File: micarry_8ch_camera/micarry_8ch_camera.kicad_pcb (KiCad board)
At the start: 2 copper layers, 127.2 x 127.2 mm, 68 parts, among them IC1 74LCX125MTCX, IC2 74LCX125MTCX, J1 MCHStreamer J3

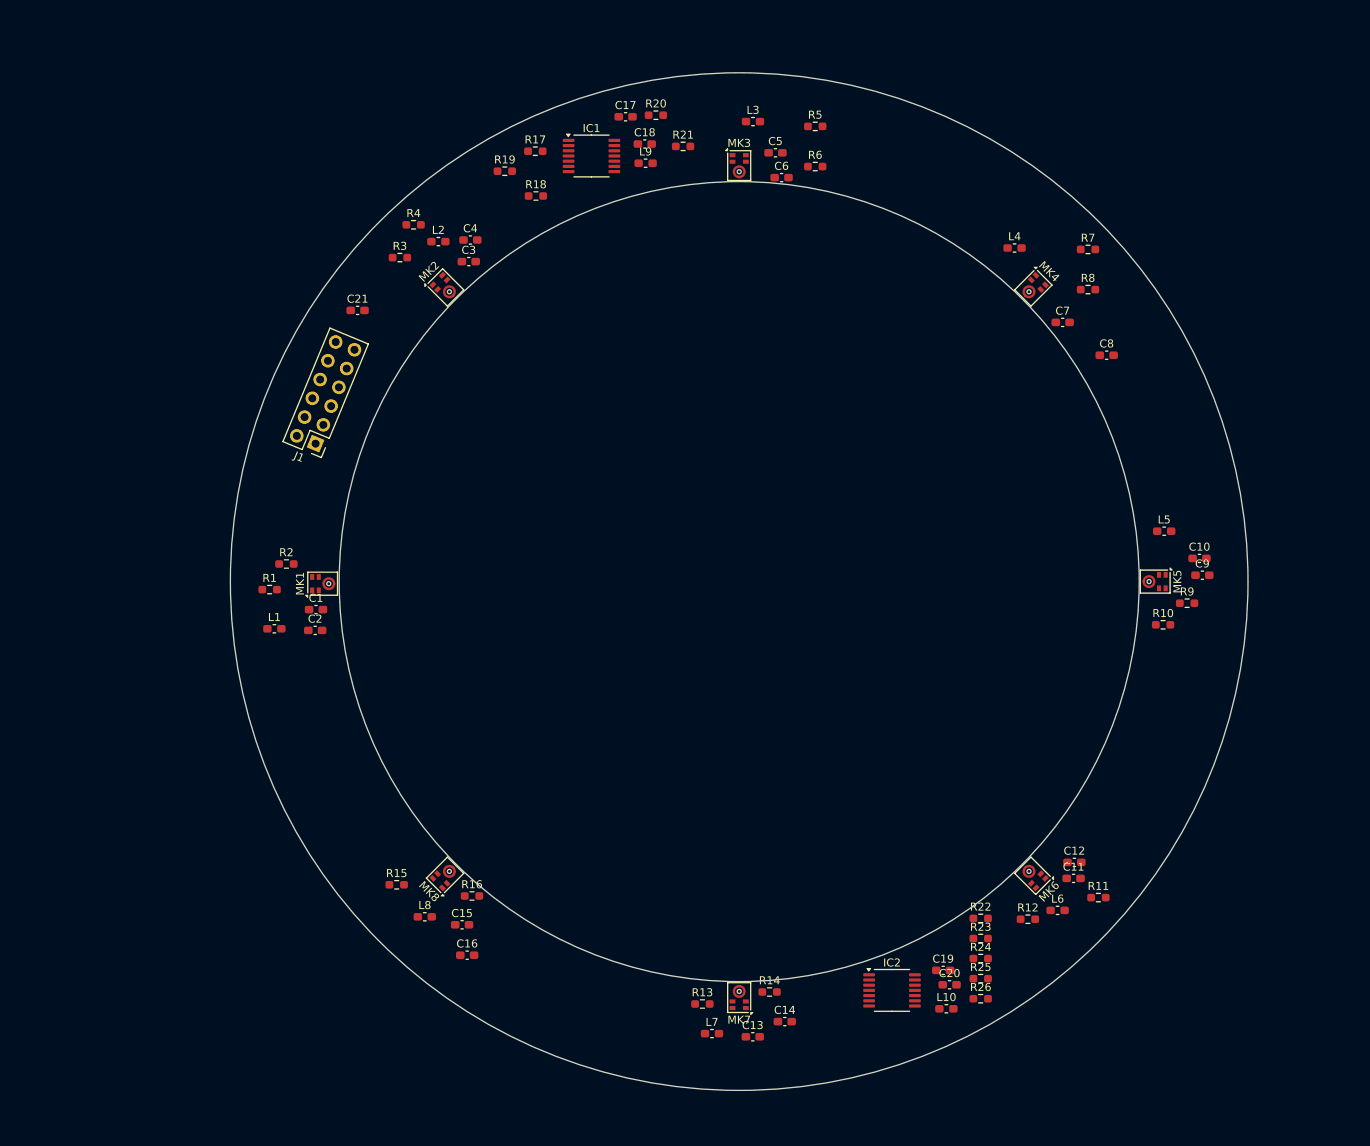
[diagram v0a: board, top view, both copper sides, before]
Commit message: 8ch progress, new mics for 16ch
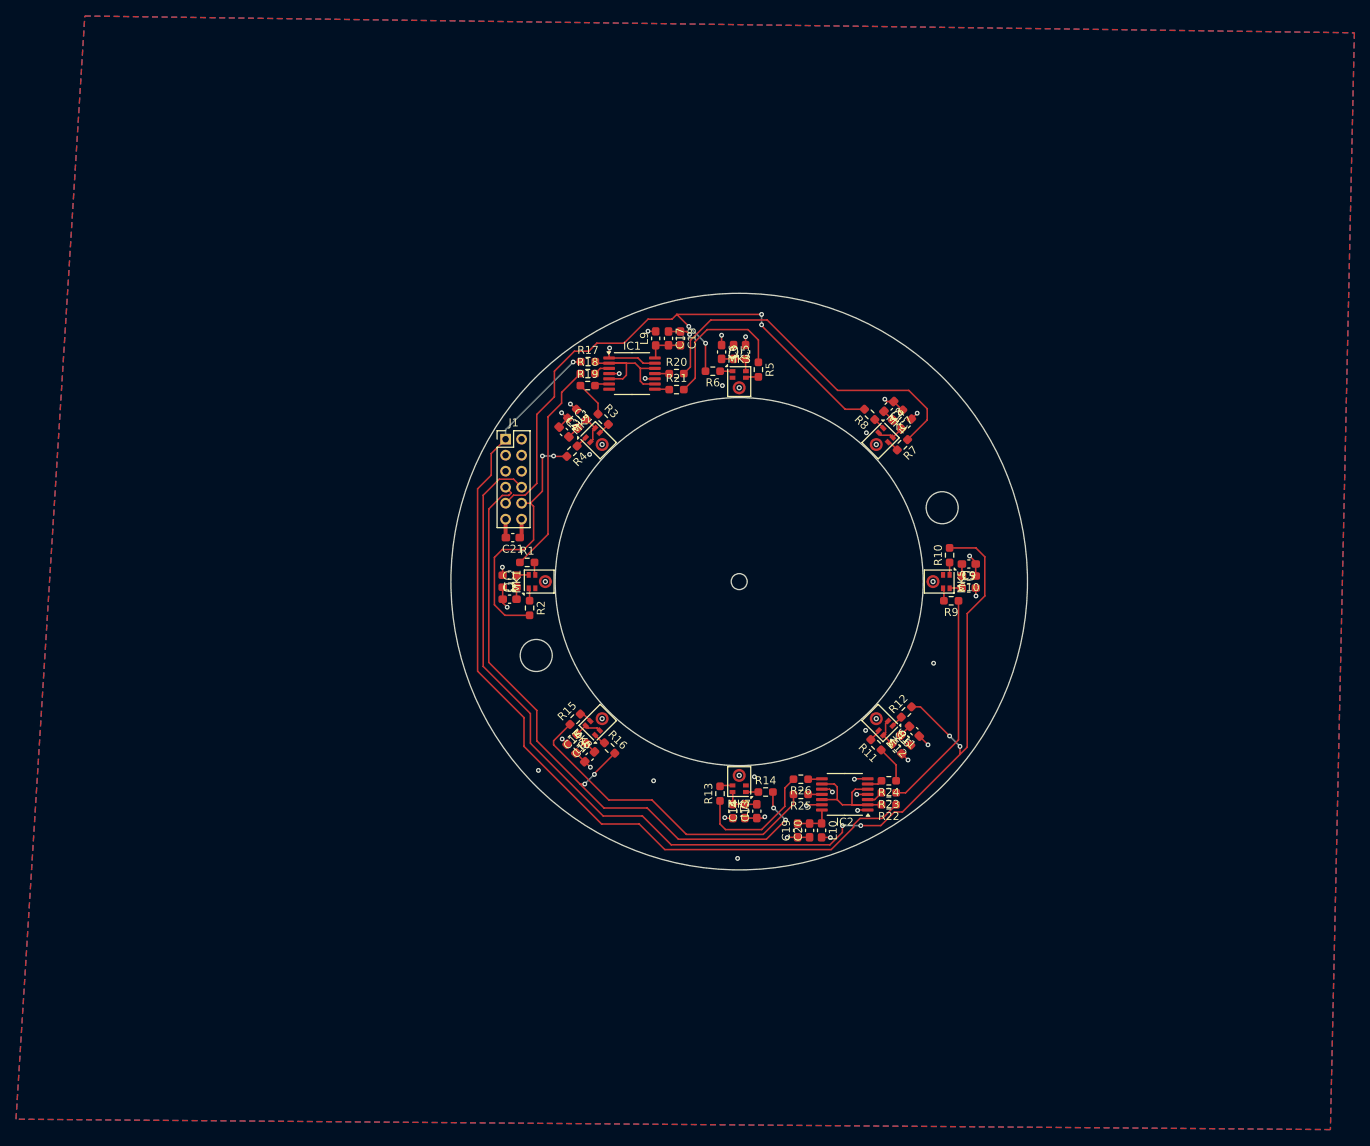
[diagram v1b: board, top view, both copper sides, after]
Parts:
- J1: footprint Connector_PinHeader_2.54mm:PinHeader_2x06_P2.54mm_Vertical -> Connector_PinHeader_2.00mm:PinHeader_2x06_P2.00mm_Vertical
- moved R26 35.5 mm to (157.7, 124.7), turned to 180 degrees
- moved R4 34.5 mm to (129.1, 83.7), turned to -135 degrees
- moved C21 34.4 mm to (121.7, 94.5), turned to 180 degrees
- moved R11 33.7 mm to (167.1, 120.4), turned to 135 degrees
- moved R7 33.7 mm to (170.4, 82.9), turned to -135 degrees
- moved R3 32.5 mm to (133.0, 79.7), turned to -45 degrees
- moved R20 32.4 mm to (142.2, 74.0)
- moved R1 32.4 mm to (123.5, 97.6)
- moved R25 32.2 mm to (157.7, 126.6), turned to 180 degrees
- moved R8 31.4 mm to (166.3, 79.1), turned to 135 degrees
- moved R5 31.2 mm to (152.4, 73.5), turned to -90 degrees
- moved R2 30.9 mm to (123.8, 103.3), turned to -90 degrees
- moved R15 30.4 mm to (129.5, 117.2), turned to 45 degrees
- moved R21 30.4 mm to (142.2, 76.0)
- moved L1 30.2 mm to (121.3, 99.2), turned to 180 degrees
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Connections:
- R18 pad 1: PDM_CLK1 -> PDM_CLK0
- R19 pad 1: PDM_CLK0 -> PDM_CLK1
- R23 pad 1: PDM_CLK5 -> PDM_CLK4
- R24 pad 1: PDM_CLK4 -> PDM_CLK5
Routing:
- net PDM_DATA2: track 0.00 -> 143.6 mm, vias 0 -> 4
- net PDM_CLK-IN: track 0.00 -> 110.7 mm, vias 0 -> 1
- net PDM_DATA3: track 0.00 -> 83.5 mm, vias 0 -> 4
- net PDM_DATA1: track 0.00 -> 75.9 mm, vias 0 -> 4
- net PDM_CLK3: track 0.00 -> 44.6 mm
- net GND: track 0.00 -> 44.4 mm, vias 0 -> 27
- net PDM_CLK7: track 0.00 -> 40.8 mm
- net PDM_DATA0: track 0.00 -> 32.1 mm, vias 0 -> 2
- net PDM_CLK4: track 0.00 -> 27.9 mm
- net PDM_CLK0: track 0.00 -> 26.7 mm
- net PDM_CLK2: track 0.00 -> 18.4 mm
- net Net-(IC1-A0): track 0.00 -> 17.4 mm
- net Net-(IC2-A0): track 0.00 -> 17.0 mm
- net PDM_CLK6: track 0.00 -> 16.3 mm
- net +3V3: track 0.00 -> 12.7 mm, vias 0 -> 10
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- added copper zone on In2.Cu, net +3V3
- added copper zone on B.Cu, net GND
- added copper zone on F.Cu, net GND
- added copper zone on In1.Cu, net GND
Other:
- board size 127.2 x 127.2 mm -> 72.1 x 72.1 mm
- copper layers 2 -> 4

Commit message: Save before dev-fork
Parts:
- MK1, MK2, MK3, MK4, MK5, MK6, MK7, MK8: value SPH1668LM4H-1 -> ~; footprint Sensor_Audio:Knowles_LGA-5_3.5x2.65mm -> ul_IM73D122V01XTMA1:PG-LLGA-5-2_INF
- moved C21 6.62 mm to (116.2, 98.1), turned to -90 degrees
- turned R1 to 180 degrees
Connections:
- C11 pad 2: Net-(MK6-SELECT) -> Net-(MK6-LR)
- C12 pad 2: Net-(MK6-SELECT) -> Net-(MK6-LR)
- C15 pad 2: Net-(MK8-SELECT) -> Net-(MK8-LR)
- C16 pad 2: Net-(MK8-SELECT) -> Net-(MK8-LR)
- C21 pad 1: +3V3 -> PDM_CLK-IN
- C3 pad 2: Net-(MK2-SELECT) -> Net-(MK2-LR)
- C4 pad 2: Net-(MK2-SELECT) -> Net-(MK2-LR)
- C7 pad 2: Net-(MK4-SELECT) -> Net-(MK4-LR)
- C8 pad 2: Net-(MK4-SELECT) -> Net-(MK4-LR)
- L2 pad 1: Net-(MK2-SELECT) -> Net-(MK2-LR)
- L4 pad 1: Net-(MK4-SELECT) -> Net-(MK4-LR)
- L6 pad 1: Net-(MK6-SELECT) -> Net-(MK6-LR)
- L8 pad 1: Net-(MK8-SELECT) -> Net-(MK8-LR)
- MK1 pad 2: GND -> Net-(MK1-VDD)
- MK1 pad 3: GND -> Net-(MK1-CLOCK)
- MK1 pad 4: Net-(MK1-CLOCK) -> GND
- MK1 pad 5: Net-(MK1-VDD) -> GND
- MK2 pad 2: Net-(MK2-SELECT) -> Net-(MK2-LR)
- MK2 pad 3: GND -> Net-(MK2-CLOCK)
- MK2 pad 4: Net-(MK2-CLOCK) -> Net-(MK2-LR)
- MK2 pad 5: Net-(MK2-SELECT) -> GND
- MK3 pad 2: GND -> Net-(MK3-VDD)
- MK3 pad 3: GND -> Net-(MK3-CLOCK)
- MK3 pad 4: Net-(MK3-CLOCK) -> GND
- MK3 pad 5: Net-(MK3-VDD) -> GND
- MK4 pad 2: Net-(MK4-SELECT) -> Net-(MK4-LR)
- MK4 pad 3: GND -> Net-(MK4-CLOCK)
- MK4 pad 4: Net-(MK4-CLOCK) -> Net-(MK4-LR)
- MK4 pad 5: Net-(MK4-SELECT) -> GND
- MK5 pad 2: GND -> Net-(MK5-VDD)
- MK5 pad 3: GND -> Net-(MK5-CLOCK)
- MK5 pad 4: Net-(MK5-CLOCK) -> GND
- MK5 pad 5: Net-(MK5-VDD) -> GND
- MK6 pad 2: Net-(MK6-SELECT) -> Net-(MK6-LR)
- MK6 pad 3: GND -> Net-(MK6-CLOCK)
- MK6 pad 4: Net-(MK6-CLOCK) -> Net-(MK6-LR)
- MK6 pad 5: Net-(MK6-SELECT) -> GND
- MK7 pad 2: GND -> Net-(MK7-VDD)
- MK7 pad 3: GND -> Net-(MK7-CLOCK)
- MK7 pad 4: Net-(MK7-CLOCK) -> GND
- MK7 pad 5: Net-(MK7-VDD) -> GND
- MK8 pad 2: Net-(MK8-SELECT) -> Net-(MK8-LR)
- MK8 pad 3: GND -> Net-(MK8-CLOCK)
- MK8 pad 4: Net-(MK8-CLOCK) -> Net-(MK8-LR)
- MK8 pad 5: Net-(MK8-SELECT) -> GND
- R1 pad 1: PDM_CLK0 -> Net-(MK1-CLOCK)
- R1 pad 2: Net-(MK1-CLOCK) -> PDM_CLK0
- R13 pad 1: PDM_CLK6 -> Net-(MK7-CLOCK)
- R13 pad 2: Net-(MK7-CLOCK) -> PDM_CLK6
- R15 pad 1: PDM_CLK7 -> Net-(MK8-CLOCK)
- R15 pad 2: Net-(MK8-CLOCK) -> PDM_CLK7
- R5 pad 1: PDM_CLK2 -> Net-(MK3-CLOCK)
- R5 pad 2: Net-(MK3-CLOCK) -> PDM_CLK2
- R7 pad 1: PDM_CLK3 -> Net-(MK4-CLOCK)
- R7 pad 2: Net-(MK4-CLOCK) -> PDM_CLK3
- R9 pad 1: PDM_CLK4 -> Net-(MK5-CLOCK)
- R9 pad 2: Net-(MK5-CLOCK) -> PDM_CLK4
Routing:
- net (no net): track 0.00 -> 20.0 mm
- net Net-(MK2-SELECT): track 6.67 -> 0.00 mm
- net Net-(MK6-SELECT): track 6.67 -> 0.00 mm
- net Net-(MK8-SELECT): track 6.67 -> 0.00 mm
- net Net-(MK4-SELECT): track 6.67 -> 0.00 mm
- net Net-(MK2-LR): track 0.00 -> 3.13 mm
- net +3V3: track 12.7 -> 10.3 mm
- net PDM_CLK-IN: track 110.7 -> 112.3 mm
- net GND: track 44.4 -> 43.2 mm, vias 27 -> 28
- net PDM_DATA3: track 83.5 -> 82.4 mm
